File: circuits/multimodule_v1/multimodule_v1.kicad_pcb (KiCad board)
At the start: 2 copper layers, 55.9 x 45.3 mm, 32 parts, among them J1 Light, J2 Temp/Hump, J3 LCDA, J4 USB_B_Micro, J5 UART, J6 BATT, J7 CO2, SW1 SW_Push, SW2 SW_Push, U1 ESP32-WROOM-32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

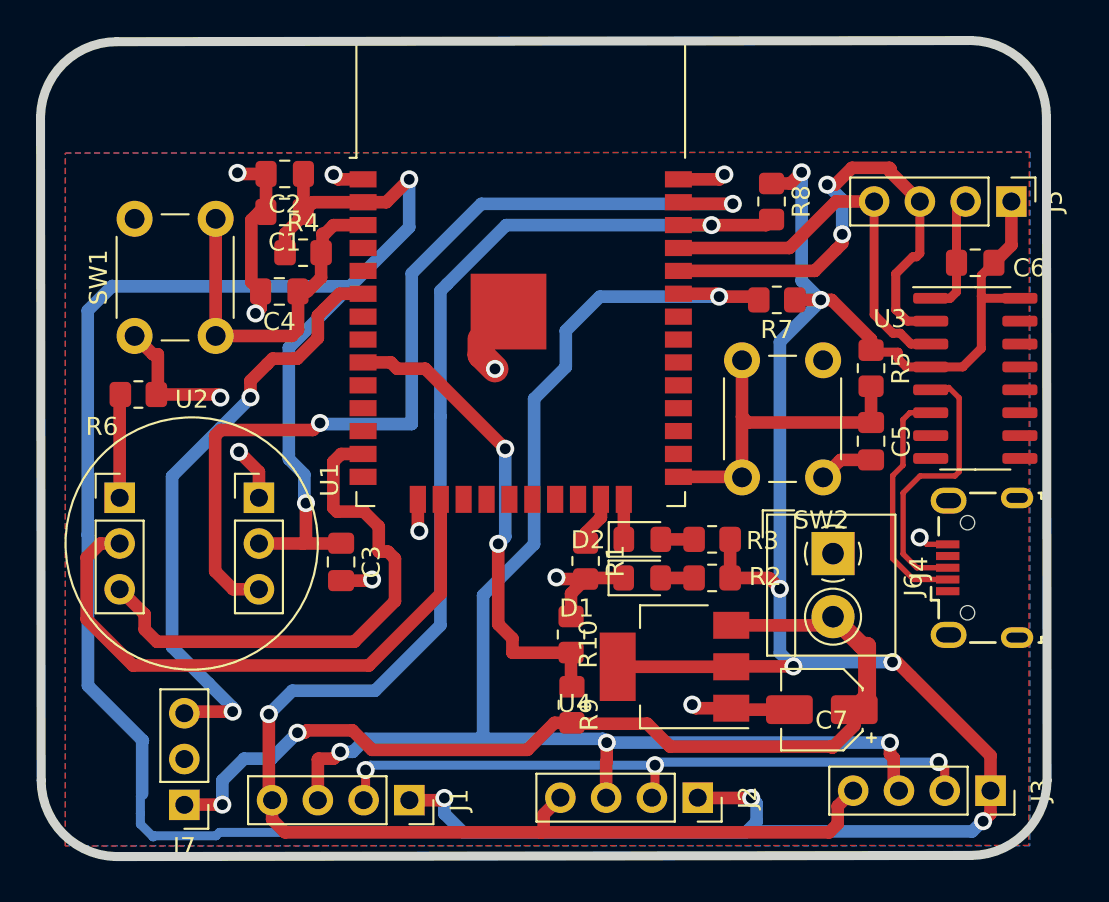
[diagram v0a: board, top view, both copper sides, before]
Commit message: Small PCB version
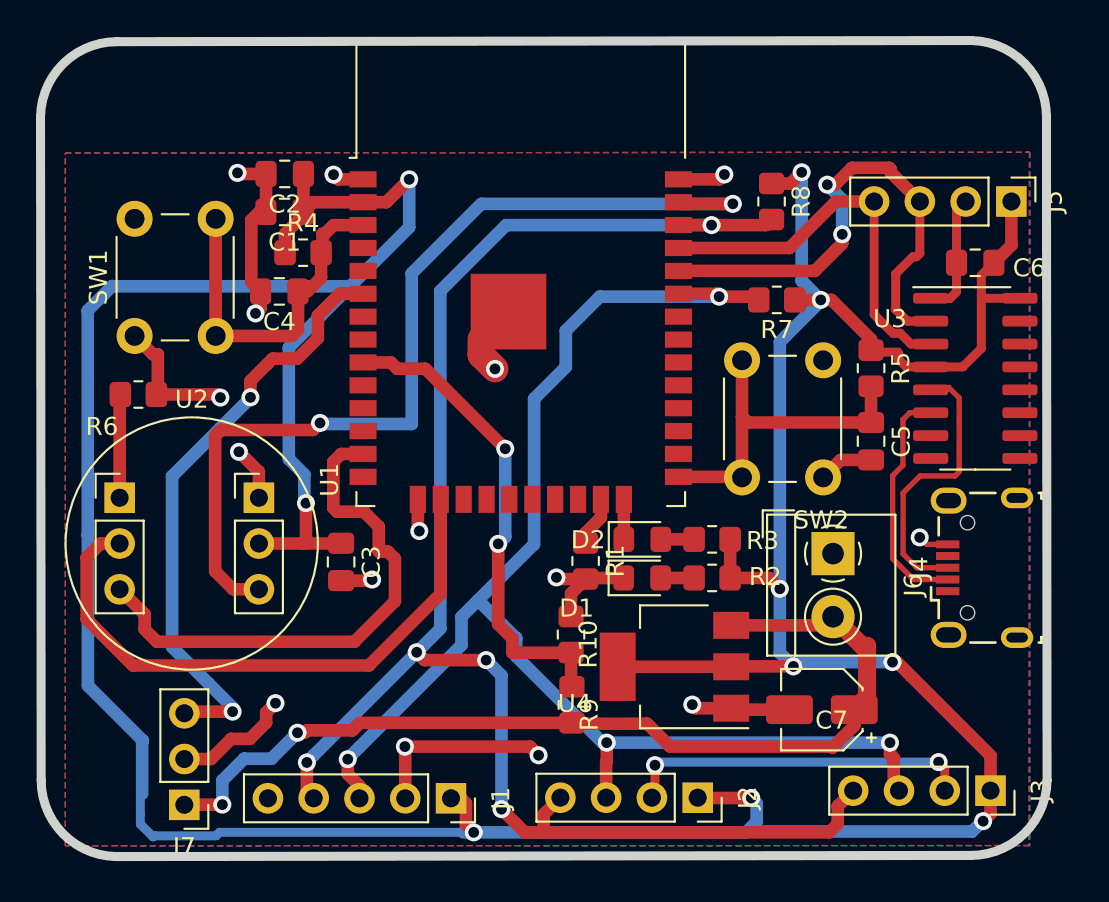
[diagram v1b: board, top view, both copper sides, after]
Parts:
- J1: value Light -> Lux; footprint Connector_PinSocket_2.54mm:PinSocket_1x04_P2.54mm_Vertical -> Connector_PinSocket_2.54mm:PinSocket_1x05_P2.54mm_Vertical
- moved J1 2.31 mm to (139.5, 128.3)
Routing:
- net I2C_SCL: track 94.3 -> 89.9 mm, vias 2 -> 5
- net VDD: track 228.3 -> 226.7 mm
- net I2C_SDA: track 79.0 -> 77.7 mm
- net GND: track 91.8 -> 90.6 mm, vias 15 -> 17
- net VCC: track 55.0 -> 54.1 mm
